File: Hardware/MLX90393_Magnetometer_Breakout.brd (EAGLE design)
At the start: 20.3 x 20.3 mm, 16 parts, among them U1 MLX90393_MAGNETOMETER

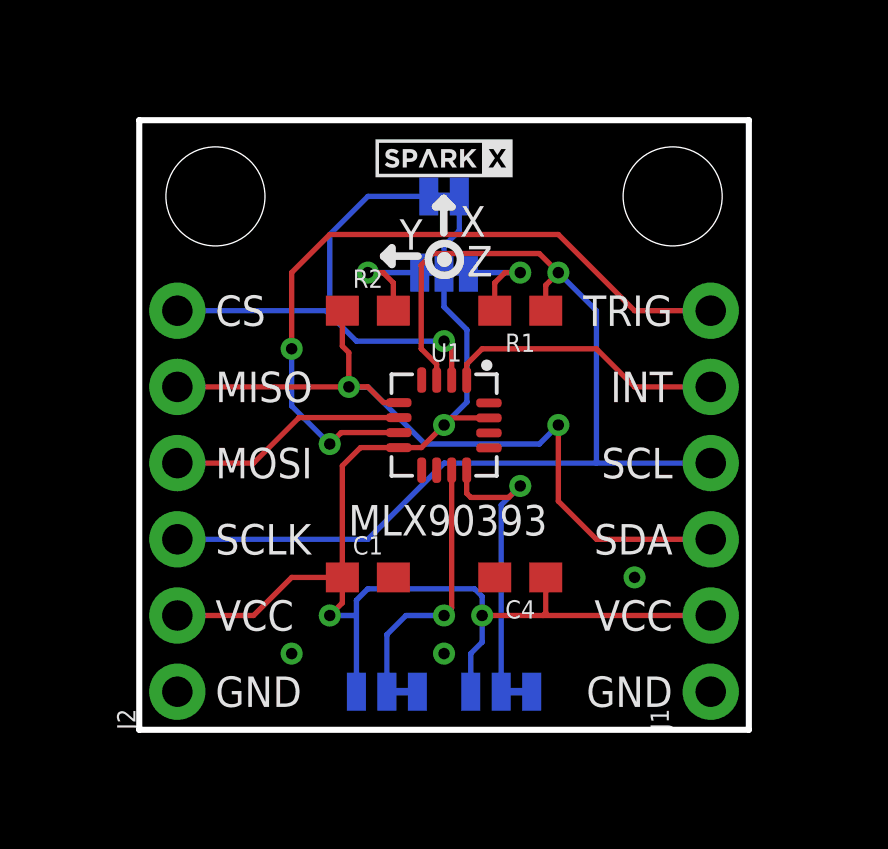
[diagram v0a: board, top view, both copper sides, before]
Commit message: fixed silk and jumper
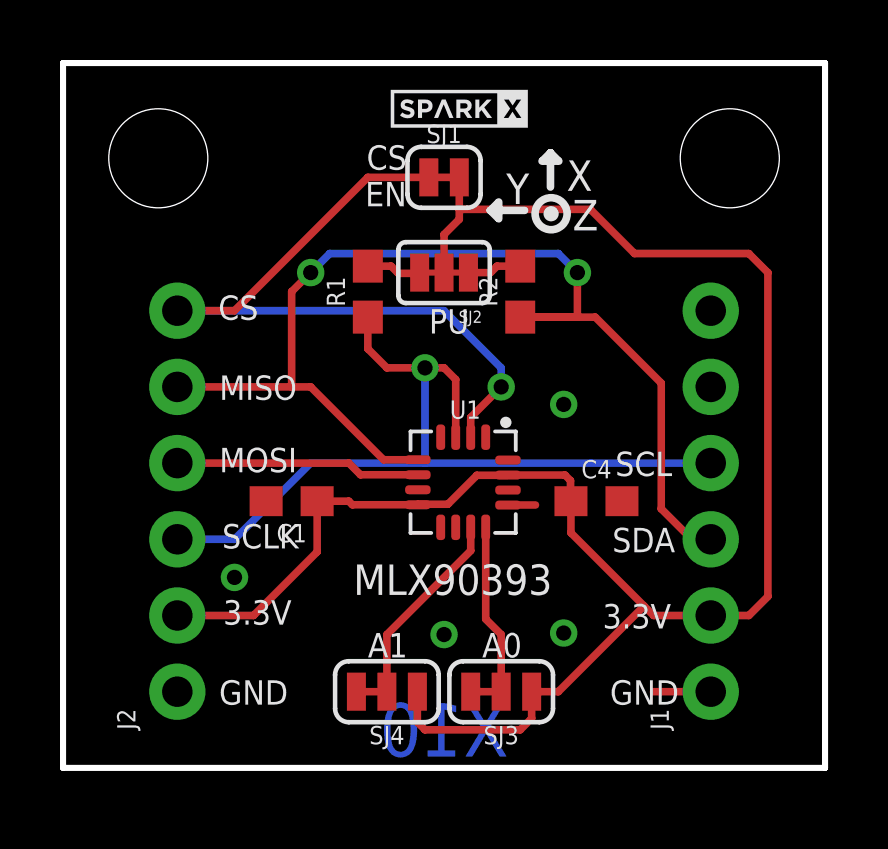
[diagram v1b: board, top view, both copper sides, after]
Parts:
- removed U$1: OSHW-LOGOS, SparkFun:OSHW-LOGO-S
- moved R1 5.12 mm to (7.62, 14.6), turned to 90 degrees
- moved R2 5.12 mm to (12.7, 14.6), turned to 90 degrees
- moved C4 3.59 mm to (15.2, 7.62), turned to 0 degrees
- moved C1 3.59 mm to (5.08, 7.62), turned to 180 degrees
- moved JP3 2.29 mm to (0.64, 19.1)
- moved JP4 2.29 mm to (19.7, 19.1)
- moved U1 2.01 mm to (10.8, 8.26)
- moved U$2 1.73 mm to (10.7, 20.7)
- moved SJ1 0.63 mm to (10.2, 18.4), flipped to the top, turned to 0 degrees
- flipped SJ2 to the top
- flipped SJ3 to the top
- flipped SJ4 to the top
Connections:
- net 3.3V renamed VDD
- net INT: no longer J1.5
- net TRIG: no longer J1.6
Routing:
- net TRIG: track 24.2 -> 0.00 mm, vias 2 -> 0
- net VDD: track 45.9 -> 62.2 mm, vias 3 -> 0
- net SDA: track 26.4 -> 37.8 mm
- net INT: track 9.40 -> 0.00 mm
- net SCL: track 36.2 -> 28.3 mm
- net CS: track 17.2 -> 24.5 mm
- net A0: track 9.89 -> 5.69 mm, vias 1 -> 0
- net GND: track 0.00 -> 2.79 mm, vias 3 -> 4
- net A1: track 9.02 -> 6.64 mm, vias 1 -> 0
- net N$4: track 3.65 -> 1.82 mm, vias 1 -> 0
- net N$5: track 3.65 -> 1.84 mm, vias 1 -> 0
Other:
- board size 20.3 x 20.3 mm -> 25.4 x 23.5 mm
- board text added: "3.3V"
- board text added: "CS EN"
- board text added: "X10"
- board text removed: "INT"
- board text removed: "J. Bartlett"
- board text removed: "TRIG"
- board text removed: "VCC"
